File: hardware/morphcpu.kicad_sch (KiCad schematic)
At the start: 80 parts, among them J1 TYPE-C-31-M-12, SW1 TS-1187A-B-A-B, U1 ICE40UP5K-SG48I, U2 FT231XS-R, U3 W25Q32JVSSIQ, U4 ME6211C33M5G-N, U5 ME6211C12M5G-N, U6 USBLC6-2SC6, X1 1532H4-16000JWPDTSNL

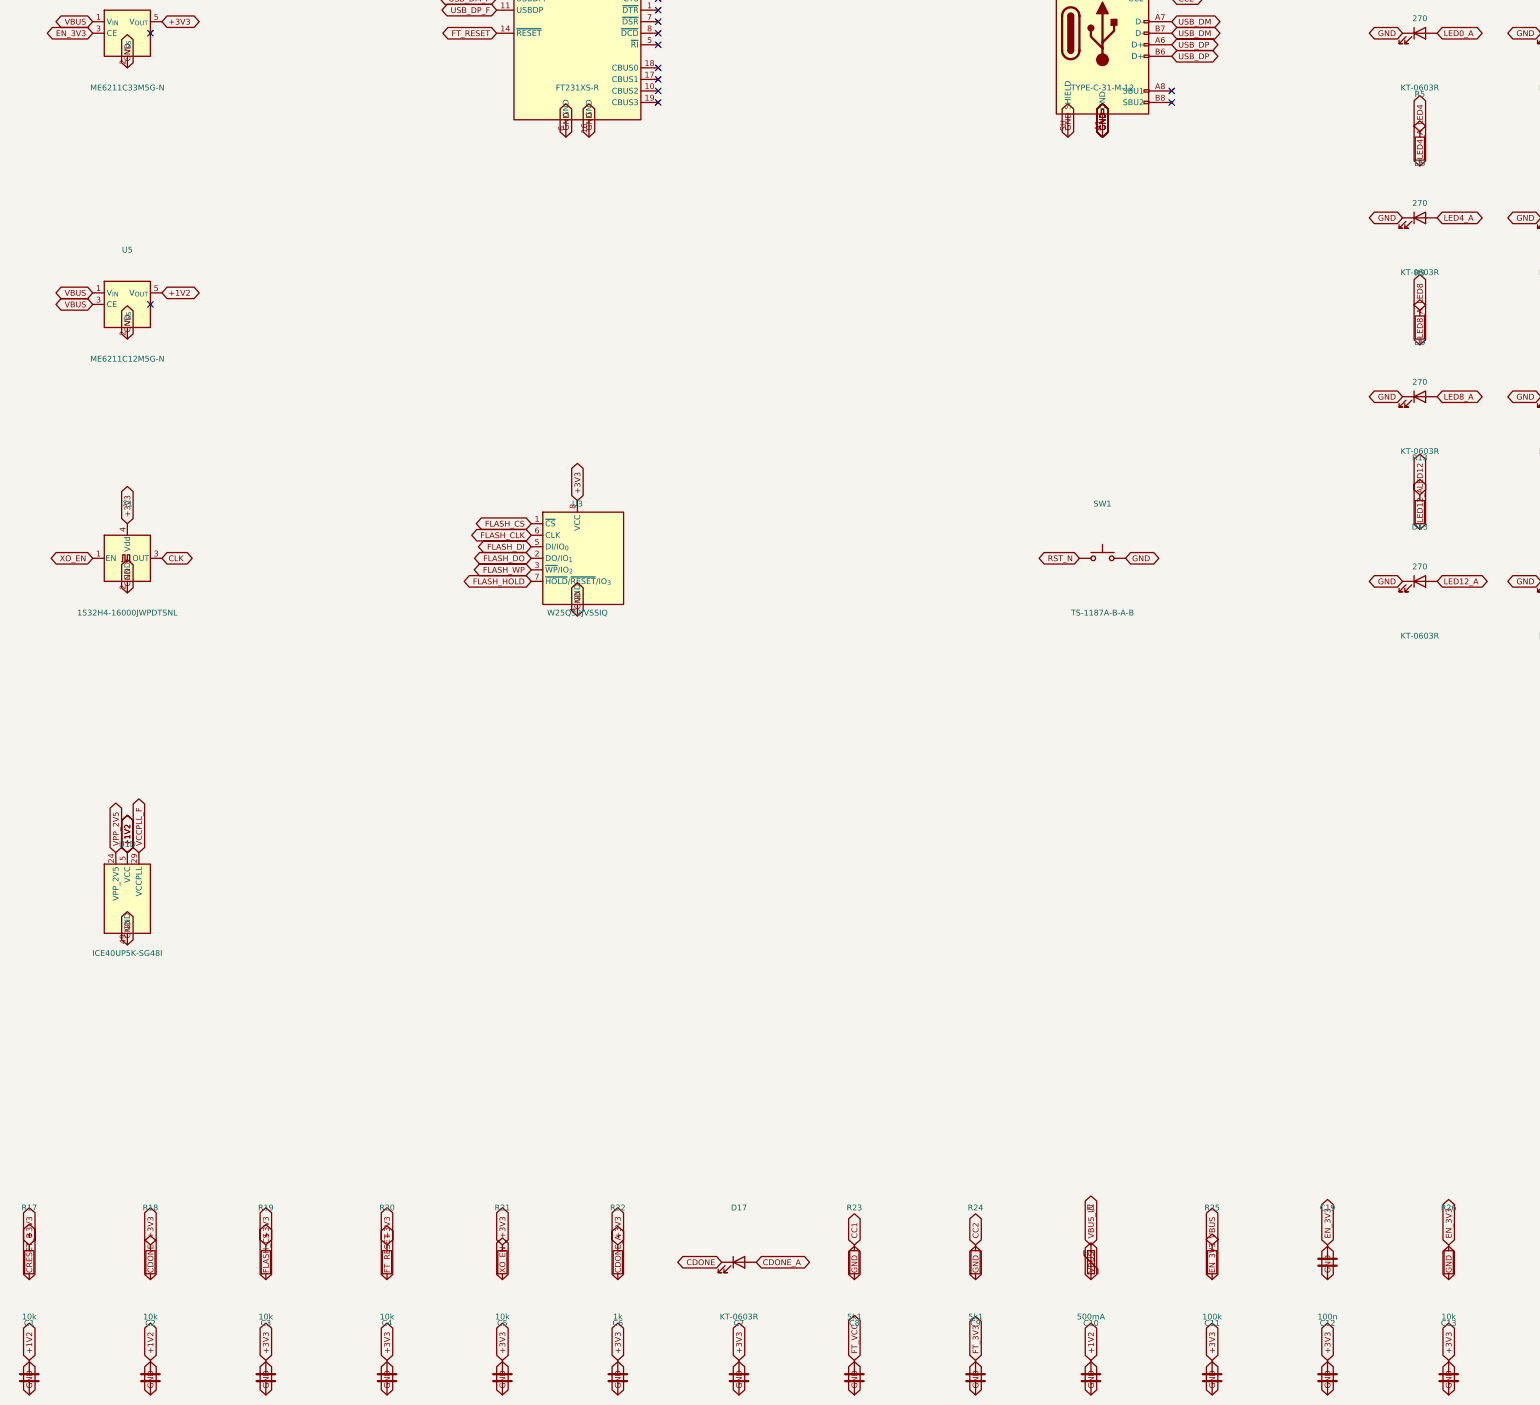
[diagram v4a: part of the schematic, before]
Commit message: 3v3 ldo to ap2112k / en bleed 10k to 1m
C82942 went to 0 stock at JLC, 11 day lead and a 196 MOQ behind it.
AP2112K-3.3TRG1 C51118 instead, 70,670 in stock, same SOT-23-5 and the same
1 VIN 2 GND 3 EN 4 NC 5 VOUT so nothing on the board moved. 600mA not 500.
couldnt get a tier out of JLC's listing, that column reads Extended for every
row including ones that arent, so its unconfirmed.

the EN RC was a divider. 100k feed against a 10k bleed put EN at
5 x 10k/110k = 0.45V, under the enable threshold of anything in this class, so
the 3V3 rail would never have come up at all. tau was 0.9ms not the 10ms this
was documented at, that figure was 100k x 100n with the bleed left out of the
sum. bleed is 1M now, C26083. EN 4.545V, tau 9.09ms.

0402 to 0402 so nothing moved, gen_pcb.py not run. all 12 gerbers identical to
the previous plot once creation dates are stripped. BOM 22 rows to 23, the 10k
row goes 9 designators to 8. ERC 0 violations, DRC 0 violations 2 unconnected.
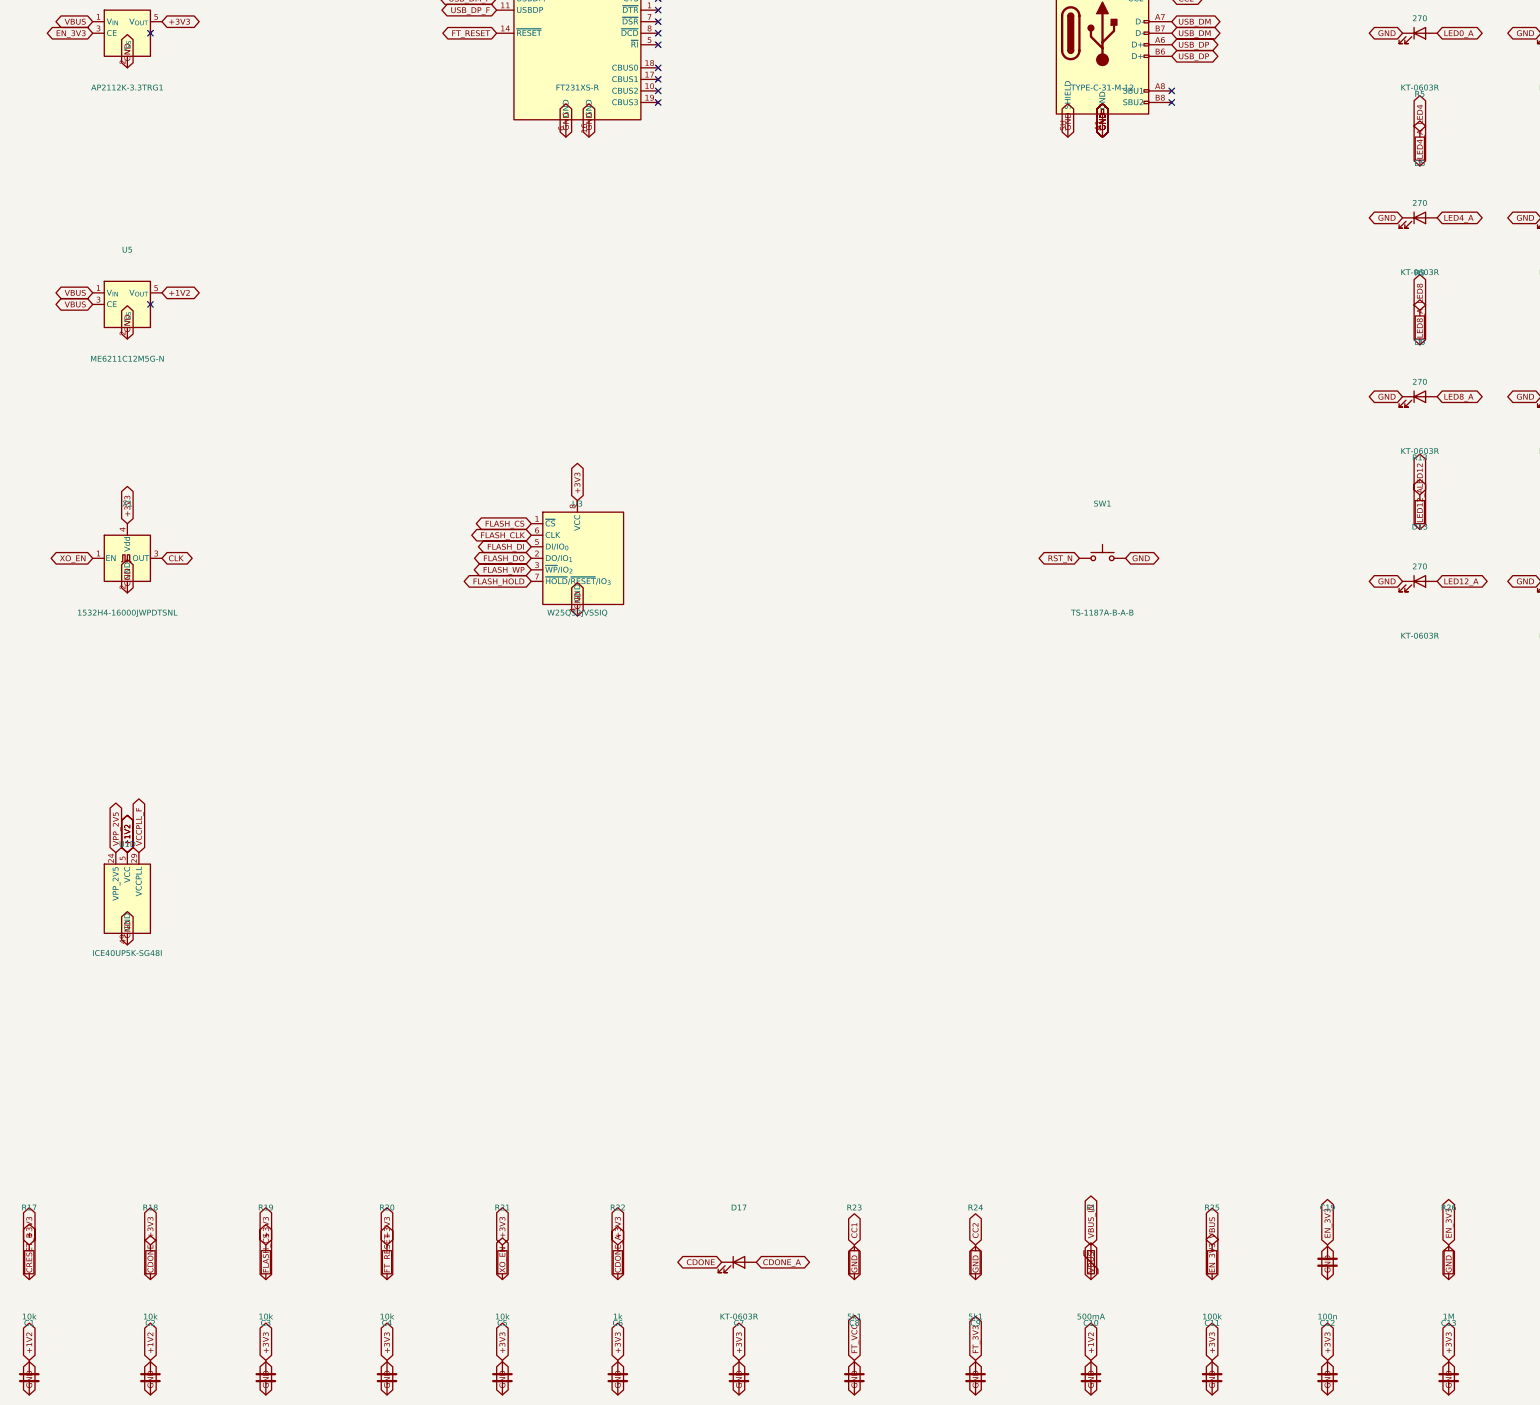
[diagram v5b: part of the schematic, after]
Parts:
- R26: value 10k -> 1M
- U4: value ME6211C33M5G-N -> AP2112K-3.3TRG1
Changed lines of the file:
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@@
 		(dnp no)
 		(property "Reference" "U4" (at 185.42 47.69 0) (effects (font (size 1.27 1.27))))
-		(property "Value" "ME6211C33M5G-N" (at 185.42 71.69 0) (effects (font (size 1.27 1.27))))
+		(property "Value" "AP2112K-3.3TRG1" (at 185.42 71.69 0) (effects (font (size 1.27 1.27))))
 		(property "Footprint" "Package_TO_SOT_SMD:SOT-23-5" (at 185.42 59.69 0) (hide yes) (effects (font (size 1.27 1.27))))
 		(instances
@@
 		(dnp no)
 		(property "Reference" "R26" (at 476.25 318.2 0) (effects (font (size 1.27 1.27))))
-		(property "Value" "10k" (at 476.25 342.2 0) (effects (font (size 1.27 1.27))))
+		(property "Value" "1M" (at 476.25 342.2 0) (effects (font (size 1.27 1.27))))
 		(property "Footprint" "Resistor_SMD:R_0402_1005Metric" (at 476.25 330.2 0) (hide yes) (effects (font (size 1.27 1.27))))
 		(instances

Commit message: 2 LEDSS!!!1!!!1!
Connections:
- net LED1: now also U1.45 (IOB_5b); no longer U1.3 (IOB_9b)
- net LED2: now also U1.42 (IOT_51a); no longer U1.23 (IOT_37a)
